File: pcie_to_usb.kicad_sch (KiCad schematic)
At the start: 45 parts, among them J14 USB-A_Samtec_USB-A-S-F-B-VT_V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, J8 USB-A_Samtec_USB-A-S-F-B-VT_V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, U2 UPD720201K8-701-BAC-A, U3 AP22615A_TSOT26, U4 AP22615A_TSOT26, U9 AP62301_TSOT

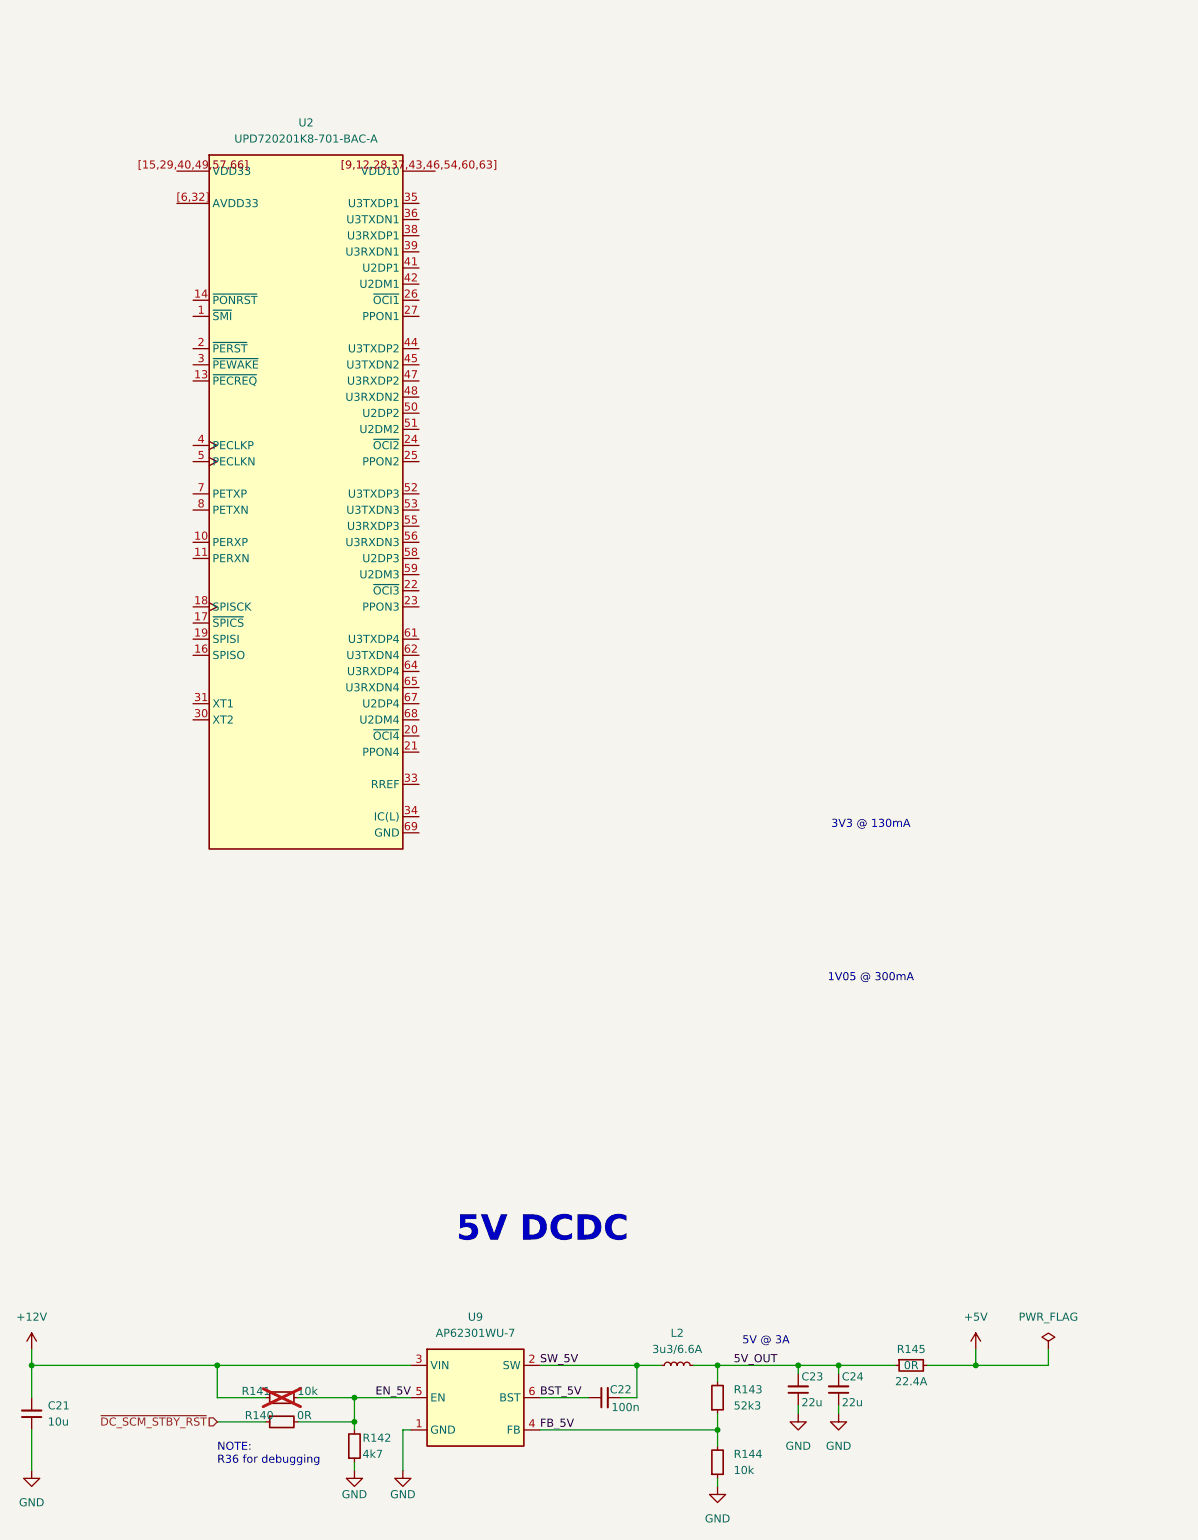
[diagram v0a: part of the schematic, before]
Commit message: [#100720] Add power section for PCIe to USB to schematic
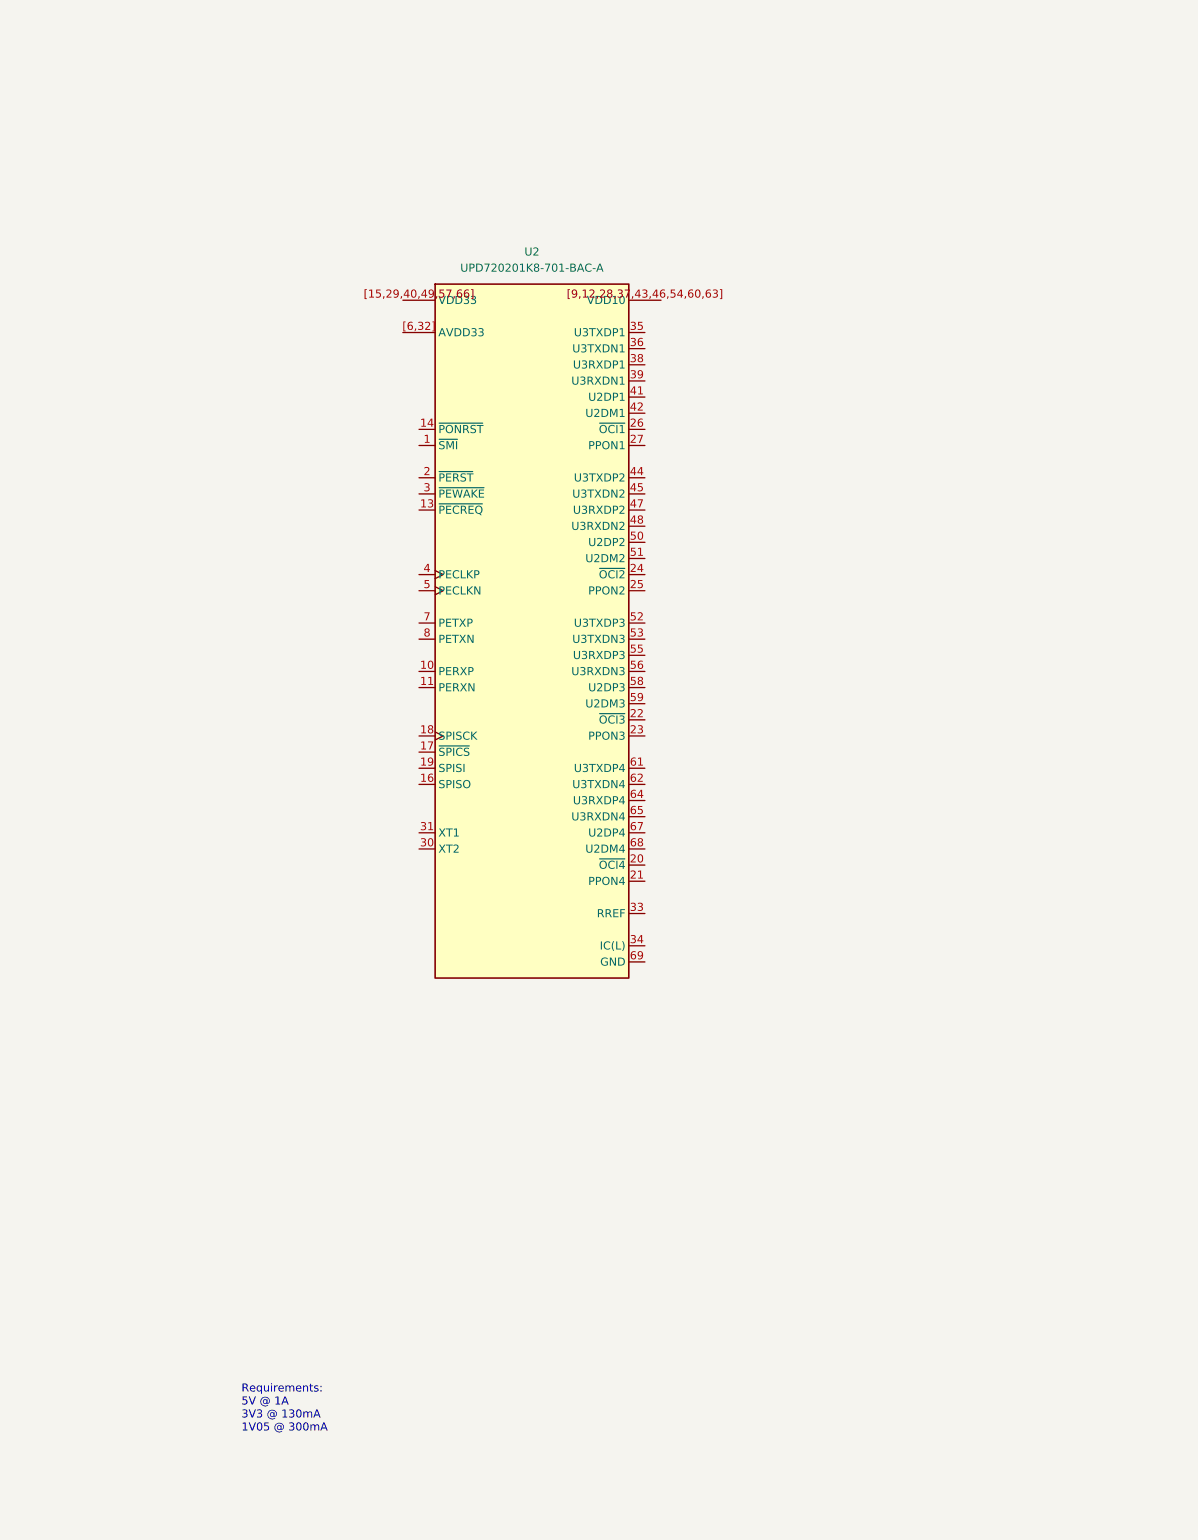
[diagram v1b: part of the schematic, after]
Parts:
- removed C21: C_10u_16V_0603, antmicro-footprints:C_0603_1608Metric, symbol antmicroCapacitors0603:C_10u_16V_0603
- removed C22: C_100n_50V_X8L_0402, antmicro-footprints:C_0402_1005Metric, symbol antmicroCapacitors0402:C_100n_50V_X8L_0402
- removed C23: C_22u_16V_0603, antmicro-footprints:C_0603_1608Metric_EIA, symbol antmicroCapacitors0603:C_22u_16V_0603
- removed C24: C_22u_0603, antmicro-footprints:C_0603_1608Metric, symbol antmicroCapacitors0603:C_22u_0603
- removed L2: L_3u3_6.6A_XEL4030, antmicro-footprints:L_Coilcraft-XEL4030, symbol antmicroFixedInductors:L_3u3_6.6A_XEL4030
- removed R140: R_0R_0402, antmicro-footprints:R_0402_1005Metric, symbol antmicroResistors0402:R_0R_0402
- removed R141, R144: R_10k_0402, antmicro-footprints:R_0402_1005Metric, symbol antmicroResistors0402:R_10k_0402
- removed R142: R_4k7_0402, antmicro-footprints:R_0402_1005Metric, symbol antmicroResistors0402:R_4k7_0402
- removed R143: R_52k3_0402, antmicro-footprints:R_0402_1005Metric, symbol antmicroResistors0402:R_52k3_0402
- removed R145: R_0R_22.4A_0603, antmicro-footprints:R_0603_1608Metric, symbol antmicroResistors0603:R_0R_22.4A_0603
- removed U9: AP62301_TSOT, antmicro-footprints:TSOT23-6, symbol antmicroDCDCConverters:AP62301_TSOT
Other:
- note added: "Requirements: 5V @ 1A 3V3 @ 130mA 1V05 @ 300mA"
- note removed: "1V05 @ 300mA"
- note removed: "3V3 @ 130mA"
- note removed: "5V @ 3A"
- note removed: "5V DCDC"
- note removed: "NOTE: R36 for debugging"
- moved on the sheet: U2

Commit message: [#100720] Start USB section
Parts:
- removed U2: UPD720201K8-701-BAC-A, antmicro-footprints:QFN-68-1EP_8x8mm_P0.4mm, symbol antmicroInterfaceControllers:UPD720201K8-701-BAC-A
- added C11, C12, C13, C14, C19, C20, C21, C22, C23, C24, C29, C30, C31: C_100n_0402, antmicro-footprints:C_0402_1005Metric, symbol antmicroCapacitors0402:C_100n_0402
- added C32, C33, C34: C_10u_10V_0402, antmicro-footprints:C_0402_1005Metric, symbol antmicroCapacitors0402:C_10u_10V_0402
- added R140: R_2k2_0402, antmicro-footprints:R_0402_1005Metric, symbol antmicroResistors0402:R_2k2_0402
- added U2: UPD720202K8-711-BAA-A, antmicro-footprints:QFN-48-1EP_7x7mm, symbol antmicroInterfaceControllers:UPD720202K8-711-BAA-A
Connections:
- net GND: now also C11.2, C12.2, C13.2, C14.2, C19.2, C20.2, C21.2, C22.2, C23.2, C24.2, C29.2, C30.2, C31.2, C32.1, C33.1, C34.1, R140.1, U2.27 (IC(L)), U2.49 (GND)
- net LOCAL_USB1.D+: now also U2.35 (U2DP1)
- net LOCAL_USB1.D-: now also U2.36 (U2DM1)
- net LOCAL_USB2.D+: now also U2.44 (U2DP2)
- net LOCAL_USB2.D-: now also U2.45 (U2DM2)
- new net: R140.2, U2.26 (RREF)
- new net +1V05: C21.1, C22.1, C23.1, C24.1, C29.1, C30.1, C31.1, C34.2, U2.[6,9,21,30,33,39,42] (VDD10)
- new net +3V3: C11.1, C12.1, C13.1, C14.1, C19.1, C20.1, C32.2, C33.2, U2.[12,22,34,43] (VDD33), U2.[3,25] (AVDD33)
- new net DC-SCM_CLK_100M_USB.CLK+: U2.1 (PECLKP)
- new net DC-SCM_CLK_100M_USB.CLK-: U2.2 (PECLKN)
- new net DC-SCM_PCIE_LOCAL_USB.RX0+: U2.7 (PERXP)
- new net DC-SCM_PCIE_LOCAL_USB.RX0-: U2.8 (PERXN)
- new net DC-SCM_PCIE_LOCAL_USB.TX0+: U2.4 (PETXP)
- new net DC-SCM_PCIE_LOCAL_USB.TX0-: U2.5 (PETXN)

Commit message: [#100720] Finish schematic after PCIe to USB addition
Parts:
- added C35, C36: C_12p_0402, antmicro-footprints:C_0402_1005Metric, symbol antmicroCapacitors0402:C_12p_0402
- added C37, C38, C39: C_100n_0402, antmicro-footprints:C_0402_1005Metric, symbol antmicroCapacitors0402:C_100n_0402
- added D8: RB521S30T1G, antmicro-footprints:SOD-523, symbol antmicroDiodesRectifiersSingle:RB521S30T1G
- added R145, R151, R152, R153, R156, R157, R158, R159, R188: R_0R_0402, antmicro-footprints:R_0402_1005Metric, symbol antmicroResistors0402:R_0R_0402
- added R154: R_1M_0402, antmicro-footprints:R_0402_1005Metric, symbol antmicroResistors0402:R_1M_0402
- added R155: R_470R_0402, antmicro-footprints:R_0402_1005Metric, symbol antmicroResistors0402:R_470R_0402
- added R160, R165, R166, R181, R182, R184, R185, R186, R187: R_10k_0402, antmicro-footprints:R_0402_1005Metric, symbol antmicroResistors0402:R_10k_0402
- added R183: R_100k_0402, antmicro-footprints:R_0402_1005Metric, symbol antmicroResistors0402:R_100k_0402
- added R189, R190, R191, R192: R_50R_0402, antmicro-footprints:R_0402_1005Metric, symbol antmicroResistors0402:R_50R_0402
- added TP11, TP12, TP13, TP14, TP15: TP_0.75mm_SMD, antmicro-footprints:TP_SMD_0.75mm, symbol antmicroTestPoints:TP_0.75mm_SMD
- added U5: W25Q80DV_USON, antmicro-footprints:USON-8_2x3mm_P0.5mm, symbol antmicroMemory:W25Q80DV_USON
- added Y1: Resonator_24MHz_ECX-1247, antmicro-footprints:Resonator_SMD_ECS_ECX-1247_1.6x1.2x0.3mm, symbol antmicroResonators:Resonator_24MHz_ECX-1247
- R129: now not fitted
- R146: now not fitted; now left out of the parts list
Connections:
- net +3V3: now also R129.2, R130.2, R146.2, R147.2, D8.2 (A), R160.2, R165.2, R166.2, R181.2, R182.2, R184.2, R185.2, R186.2, R187.2
- net +5V: no longer R129.2, R130.2, R146.2, R147.2
- net DC-SCM_PCIE_LOCAL_USB.TX0+: now also C37.1; no longer U2.4 (PETXP)
- net DC-SCM_PCIE_LOCAL_USB.TX0-: now also C38.1; no longer U2.5 (PETXN)
- net GND: now also C35.1, C36.1, C39.2, R183.1, R189.2, R190.2, R191.2, R192.2, U5.4 (VSS), U5.EP, Y1.2 (SH), Y1.4 (SH)
- net USBA1_5V_PEN: now also R151.2
- net USBA1_FLG: now also R145.2
- net USBA2_5V_PEN: now also R153.2
- net USBA2_FLG: now also R152.2
- net ~{PECREQ}: now reaches U2.10 (~{PECREQ})
- net ~{PECREQ}: now also R186.1, TP11.1
- net at U2.11 (~{PONRST}): now also R187.1, R188.1, TP15.1
- net USB_FLASH_SPI.DO: now reaches U2.13 (SPISO)
- net USB_FLASH_SPI.DO: now also R156.1
- net USB_FLASH_SPI.~{CS0}: now reaches U2.14 (~{SPICS})
- net USB_FLASH_SPI.~{CS0}: now also R159.1
- net USB_FLASH_SPI.SCK: now reaches U2.15 (SPISCK)
- net USB_FLASH_SPI.SCK: now also R158.1
- net USB_FLASH_SPI.DI: now reaches U2.16 (SPISI)
- net USB_FLASH_SPI.DI: now also R157.1
- net ~{OCI1}: now reaches U2.17 (~{OCI2})
- net ~{OCI1}: now also U2.19 (~{OCI1}), R145.1, R152.1
- net PPON1: now reaches U2.18 (PPON2)
- net PPON1: now also U2.20 (PPON1), R151.1, R153.1
- net XT2: now reaches U2.23 (XT2)
- net XT2: now also R155.2
- net XT1: now reaches U2.24 (XT1)
- net XT1: now also C35.2, R154.2, Y1.1
- net at U2.31 (U3RXDP1): now also R189.1
- net at U2.32 (U3RXDN1): now also R190.1
- net at U2.40 (U3RXDP2): now also R191.1
- net at U2.41 (U3RXDN2): now also R192.1
- net ~{SMI}: now reaches U2.46 (~{SMI})
- net ~{SMI}: now also R184.1, TP13.1
- net ~{PCIE_HPM_SCM_PERST}: now reaches U2.47 (~{PERST})
- net ~{PCIE_HPM_SCM_PERST}: now also TP14.1
- net ~{PEWAKE}: now reaches U2.48 (~{PEWAKE})
- net ~{PEWAKE}: now also R185.1, TP12.1
- new net: C36.2, R154.1, R155.1, Y1.3
- new net +3V3_FLASH: C39.1, D8.1 (C), U5.8 (VCC)
- new net PETX+: C37.2, U2.4 (PETXP)
- new net PETX-: C38.2, U2.5 (PETXN)
- new net SPI_CLK: R158.2, R183.2, U5.6 (SCLK)
- new net SPI_DI: R157.2, R165.1, U5.2 (SO/IO1)
- new net SPI_DO: R156.2, R160.1, U5.5 (SI/IO0)
- new net ~{DC_SCM_STBY_RST}: R188.2
- new net ~{HOLD}: R181.1, U5.7 (~{HOLD}/IO3)
- new net ~{SPI_CS}: R159.2, R182.1, U5.1 (~{CS})
- new net ~{WP}: R166.1, U5.3 (~{WP}/IO2)
- no-connect marks 0 -> 4
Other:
- note added: "Configuration flash"
- note added: "PCIe to USB controller"
- note removed: "Requirements: 5V @ 1A 3V3 @ 130mA 1V05 @ 300mA"
- moved on the sheet: C10, C11, C12, C13, C14, C19, C20, C21, C22, C23, C24, C29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

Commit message: [#100720] Clear ERC
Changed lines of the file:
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@@
 			(font
 				(size 4 4)
-				(thickness 0.5994)
+				(thickness 0.8)
 				(bold yes)
 			)
@@
 			(font
 				(size 4 4)
-				(thickness 0.5994)
+				(thickness 0.8)
 				(bold yes)
 			)
@@
 	(text "USB1 2.0"
 		(exclude_from_sim no)
-		(at 304.8 34.29 0)
+		(at 304.8 38.1 0)
 		(effects
 			(font
 				(size 4 4)
-				(thickness 0.5994)
+				(thickness 0.8)
 				(bold yes)
 			)
@@
 			(font
 				(size 4 4)
-				(thickness 0.5994)
+				(thickness 0.8)
 				(bold yes)
 			)
@@
 			)
 		)
-		(property "Datasheet" "https://4donline.ihs.com/images/VipMasterIC/IC/RNCC/RNCCS17404/RNCCS17404-1.pdf"
+		(property "Datasheet" "https://www.renesas.com/en/document/dst/pd720201-pd720202-datasheet"
 			(at 180.34 107.95 0)
 			(hide yes)
